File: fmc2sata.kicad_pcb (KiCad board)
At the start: 4 copper layers, 108 x 69 mm, 58 parts, among them J1 ASP-134488-01, J2 1-2199230-6, J3 te-770829-1, Q1 BSS138APW, Q2 BSS138APW, Q3 DMG2305UX-13, Q4 BSS138APW, U1 TPS565208, U2 TPS565208, Y1 AX3DAF1-150.0000

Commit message: Component cleanup
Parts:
- C1, C2, C3, C6, C7, C8: footprint antmicro-footprints:0603-cap -> fmc2sata-footprints:0603-cap
- C10, C4, C5, C9: footprint antmicro-footprints:0805-cap -> fmc2sata-footprints:0805-cap
- D1, D2, D3, D4, D5: footprint antmicro-footprints:LED_0603 -> fmc2sata-footprints:LED_0603
- J1: footprint antmicro-footprints:ASP-134488-01 -> fmc2sata-footprints:ASP-134488-01
- J2: footprint antmicro-footprints:1-2199230-6 -> fmc2sata-footprints:1-2199230-6
- J3: footprint antmicro-footprints:te-770829-1 -> fmc2sata-footprints:te-770829-1
- L1: footprint antmicro-footprints:WE_74437336022 -> fmc2sata-footprints:WE_74437336022
- L2: footprint antmicro-footprints:WE_74437336033 -> fmc2sata-footprints:WE_74437336033
- N1: footprint antmicro-footprints:antmicro-logo_scaled_20mm -> fmc2sata-footprints:antmicro-logo_scaled_20mm
- N2: footprint antmicro-footprints:oshw-logo -> fmc2sata-footprints:oshw-logo
- Q1, Q2, Q4: footprint antmicro-footprints:SC70-3 -> fmc2sata-footprints:SC70-3
- Q3: footprint antmicro-footprints:SOT-23-3 -> fmc2sata-footprints:SOT-23-3
- R1, R11, R12, R13, R17, R18, R19, R21, R22, R3, R4, R6, R7, R9: footprint antmicro-footprints:0402-res -> fmc2sata-footprints:0402-res
- SP1, SP2: footprint antmicro-footprints:9774025151 -> fmc2sata-footprints:9774025151
- U1, U2: footprint antmicro-footprints:SOT-23-6 -> fmc2sata-footprints:SOT-23-6
- Y1: footprint antmicro-footprints:AX3DAF1 -> fmc2sata-footprints:AX3DAF1

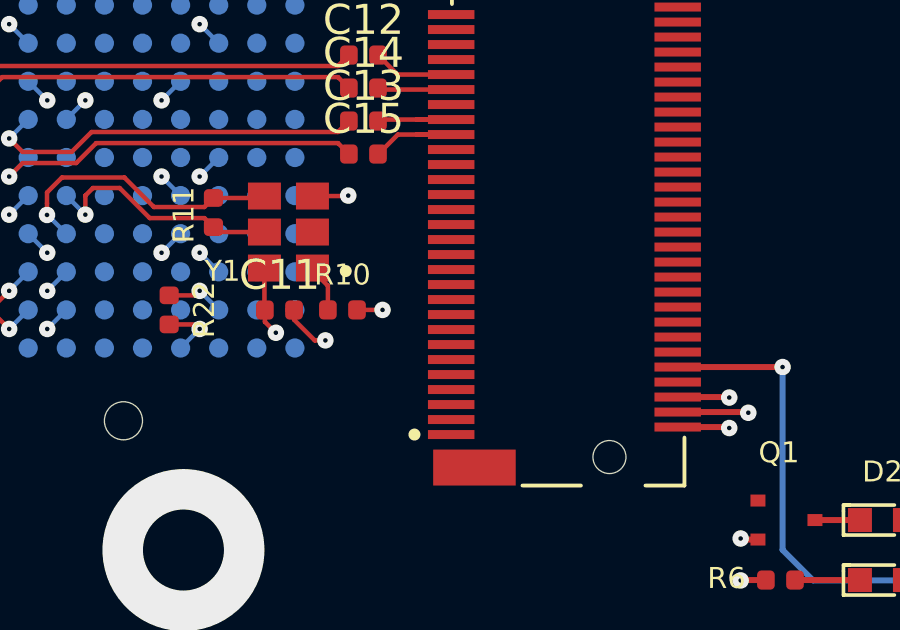
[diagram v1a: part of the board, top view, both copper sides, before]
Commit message: Update local libraries
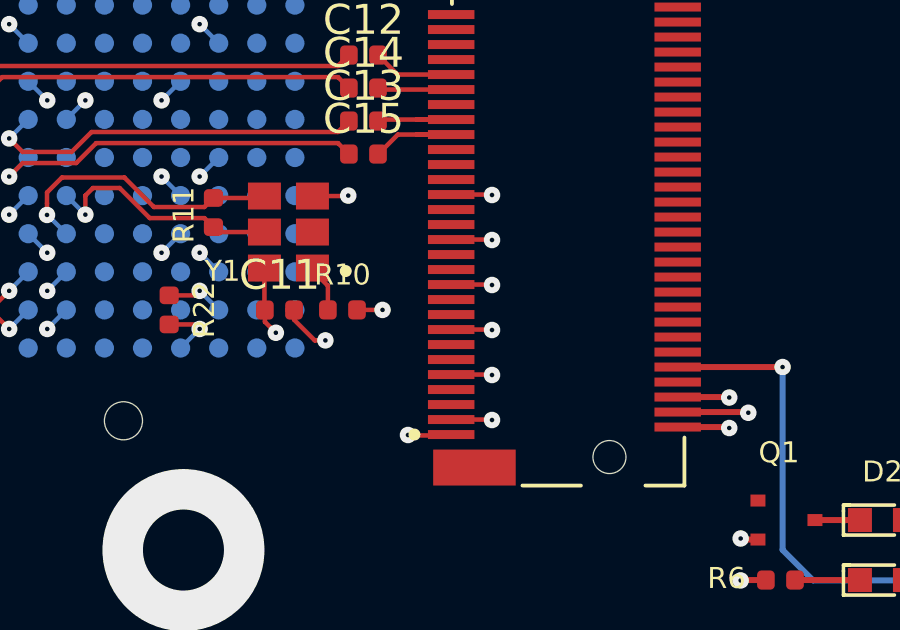
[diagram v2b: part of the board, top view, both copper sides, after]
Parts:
- C11, C12, C13, C14, C15: footprint antmicro-footprints:0402-cap -> fmc2sata-footprints:0402-cap
- R10, R14, R15, R16, R2, R20, R5, R8: footprint antmicro-footprints:0402-res -> fmc2sata-footprints:0402-res
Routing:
- net GND: track 69.0 -> 78.5 mm, vias 117 -> 124
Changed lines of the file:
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@@
     (thickness 1.6)
     (drawings 13)
-    (tracks 439)
+    (tracks 454)
     (zones 0)
     (modules 58)
@@
     (add_net SATA_CLK_P)
   )
-  (module antmicro-footprints:0402-res (layer F.Cu)
+  (module fmc2sata-footprints:0402-res (layer F.Cu)
     (at 128.606 66.424 270)
     (descr "Resistor SMD 0402 (1005 Metric), square (rectangular) end terminal, IPC_7351 nominal, (Body size source: http://www.tortai-tech.com/upload/download/2011102023233369053.pdf), generated with kicad-footprint-generator")
@@
     )
   )
-  (module antmicro-footprints:0402-res (layer F.Cu)
+  (module fmc2sata-footprints:0402-res (layer F.Cu)
     (at 105.3 66.7)
     (descr "Resistor SMD 0402 (1005 Metric), square (rectangular) end terminal, IPC_7351 nominal, (Body size source: http://www.tortai-tech.com/upload/download/2011102023233369053.pdf), generated with kicad-footprint-generator")
@@
     )
   )
-  (module antmicro-footprints:0402-res (layer F.Cu)
+  (module fmc2sata-footprints:0402-res (layer F.Cu)
     (at 105.3 68.7 180)
     (descr "Resistor SMD 0402 (1005 Metric), square (rectangular) end terminal, IPC_7351 nominal, (Body size source: http://www.tortai-tech.com/upload/download/2011102023233369053.pdf), generated with kicad-footprint-generator")
@@
     )
   )
-  (module antmicro-footprints:0402-res (layer F.Cu)
+  (module fmc2sata-footprints:0402-res (layer F.Cu)
     (at 105.3 69.8)
     (descr "Resistor SMD 0402 (1005 Metric), square (rectangular) end terminal, IPC_7351 nominal, (Body size source: http://www.tortai-tech.com/upload/download/2011102023233369053.pdf), generated with kicad-footprint-generator")
@@
     )
   )
-  (module antmicro-footprints:0402-res (layer F.Cu)
+  (module fmc2sata-footprints:0402-res (layer F.Cu)
     (at 87.9 101.095)
     (descr "Resistor SMD 0402 (1005 Metric), square (rectangular) end terminal, IPC_7351 nominal, (Body size source: http://www.tortai-tech.com/upload/download/2011102023233369053.pdf), generated with kicad-footprint-generator")
@@
     )
   )
-  (module antmicro-footprints:0402-res (layer F.Cu)
+  (module fmc2sata-footprints:0402-res (layer F.Cu)
     (at 85.6 84.9)
     (descr "Resistor SMD 0402 (1005 Metric), square (rectangular) end terminal, IPC_7351 nominal, (Body size source: http://www.tortai-tech.com/upload/download/2011102023233369053.pdf), generated with kicad-footprint-generator")
@@
     )
   )
-  (module antmicro-footprints:0402-res (layer F.Cu)
+  (module fmc2sata-footprints:0402-res (layer F.Cu)
     (at 99.5 62.47 90)
     (descr "Resistor SMD 0402 (1005 Metric), square (rectangular) end terminal, IPC_7351 nominal, (Body size source: http://www.tortai-tech.com/upload/download/2011102023233369053.pdf), generated with kicad-footprint-generator")
@@
     )
   )
-  (module antmicro-footprints:0402-res (layer F.Cu)
+  (module fmc2sata-footprints:0402-res (layer F.Cu)
     (at 99.63 76.51 90)
     (descr "Resistor SMD 0402 (1005 Metric), square (rectangular) end terminal, IPC_7351 nominal, (Body size source: http://www.tortai-tech.com/upload/download/2011102023233369053.pdf), generated with kicad-footprint-generator")
@@
     )
   )
-  (module antmicro-footprints:0402-cap (layer F.Cu)
+  (module fmc2sata-footprints:0402-cap (layer F.Cu)
     (at 88.6 95.9)
     (descr "Resistor SMD 0402 (1005 Metric), square (rectangular) end terminal, IPC_7351 nominal, (Body size source: http://www.tortai-tech.com/upload/download/2011102023233369053.pdf), generated with kicad-footprint-generator")
@@
     )
   )
-  (module antmicro-footprints:0402-cap (layer F.Cu)
+  (module fmc2sata-footprints:0402-cap (layer F.Cu)
     (at 88.6 93.7)
     (descr "Resistor SMD 0402 (1005 Metric), square (rectangular) end terminal, IPC_7351 nominal, (Body size source: http://www.tortai-tech.com/upload/download/2011102023233369053.pdf), generated with kicad-footprint-generator")
@@
     )
   )
-  (module antmicro-footprints:0402-cap (layer F.Cu)
+  (module fmc2sata-footprints:0402-cap (layer F.Cu)
     (at 88.6 94.8)
     (descr "Resistor SMD 0402 (1005 Metric), square (rectangular) end terminal, IPC_7351 nominal, (Body size source: http://www.tortai-tech.com/upload/download/2011102023233369053.pdf), generated with kicad-footprint-generator")
@@
     )
   )
-  (module antmicro-footprints:0402-cap (layer F.Cu)
+  (module fmc2sata-footprints:0402-cap (layer F.Cu)
     (at 88.6 92.6)
     (descr "Resistor SMD 0402 (1005 Metric), square (rectangular) end terminal, IPC_7351 nominal, (Body size source: http://www.tortai-tech.com/upload/download/2011102023233369053.pdf), generated with kicad-footprint-generator")
@@
     )
   )
-  (module antmicro-footprints:0402-cap (layer F.Cu)
+  (module fmc2sata-footprints:0402-cap (layer F.Cu)
     (at 85.8 101.1)
     (descr "Resistor SMD 0402 (1005 Metric), square (rectangular) end terminal, IPC_7351 nominal, (Body size source: http://www.tortai-tech.com/upload/download/2011102023233369053.pdf), generated with kicad-footprint-generator")
@@
   (via (at 132.602 46.1) (size 5.4) (drill 2.7) (layers F.Cu B.Cu) (net 0))
   (via (at 132.6 109.1) (size 5.5) (drill 2.7) (layers F.Cu B.Cu) (net 0))
+  (via (at 90.085 105.265) (size 0.55) (drill 0.15) (layers F.Cu B.Cu) (net 2))
+  (segment (start 91.445 105.28) (end 90.1 105.28) (width 0.15) (layer F.Cu) (net 2))
+  (via (at 92.885 104.765) (size 0.55) (drill 0.15) (layers F.Cu B.Cu) (net 2))
+  (segment (start 91.525 104.75) (end 92.87 104.75) (width 0.15) (layer F.Cu) (net 2))
+  (via (at 92.885 103.265) (size 0.55) (drill 0.15) (layers F.Cu B.Cu) (net 2))
+  (segment (start 91.525 103.25) (end 92.87 103.25) (width 0.15) (layer F.Cu) (net 2))
+  (via (at 92.885 101.765) (size 0.55) (drill 0.15) (layers F.Cu B.Cu) (net 2))
+  (segment (start 91.525 101.75) (end 92.87 101.75) (width 0.15) (layer F.Cu) (net 2))
+  (via (at 92.885 100.265) (size 0.55) (drill 0.15) (layers F.Cu B.Cu) (net 2))
+  (segment (start 91.525 100.25) (end 92.87 100.25) (width 0.15) (layer F.Cu) (net 2))
+  (via (at 92.885 98.765) (size 0.55) (drill 0.15) (layers F.Cu B.Cu) (net 2))
+  (segment (start 91.525 98.75) (end 92.87 98.75) (width 0.15) (layer F.Cu) (net 2))
   (segment (start 77.425 54.105) (end 76.79 53.47) (width 0.15) (layer B.Cu) (net 1))
   (via (at 76.79 53.47) (size 0.55) (drill 0.15) (layers F.Cu B.Cu) (net 1))
@@
   (segment (start 126.64 69.25) (end 127.177 69.25) (width 0.15) (layer F.Cu) (net 2))
   (segment (start 127.177 69.25) (end 127.209 69.218) (width 0.15) (layer F.Cu) (net 2))
+  (via (at 92.885 97.265) (size 0.55) (drill 0.15) (layers F.Cu B.Cu) (net 2))
+  (segment (start 91.525 97.25) (end 92.87 97.25) (width 0.15) (layer F.Cu) (net 2))
+  (segment (start 92.87 97.25) (end 92.885 97.265) (width 0.15) (layer F.Cu) (net 2))
   (segment (start 94.85 76.03) (end 93.85 76.03) (width 0.5) (layer F.Cu) (net 3))
   (segment (start 95.16 75.72) (end 94.85 76.03) (width 0.5) (layer F.Cu) (net 3))

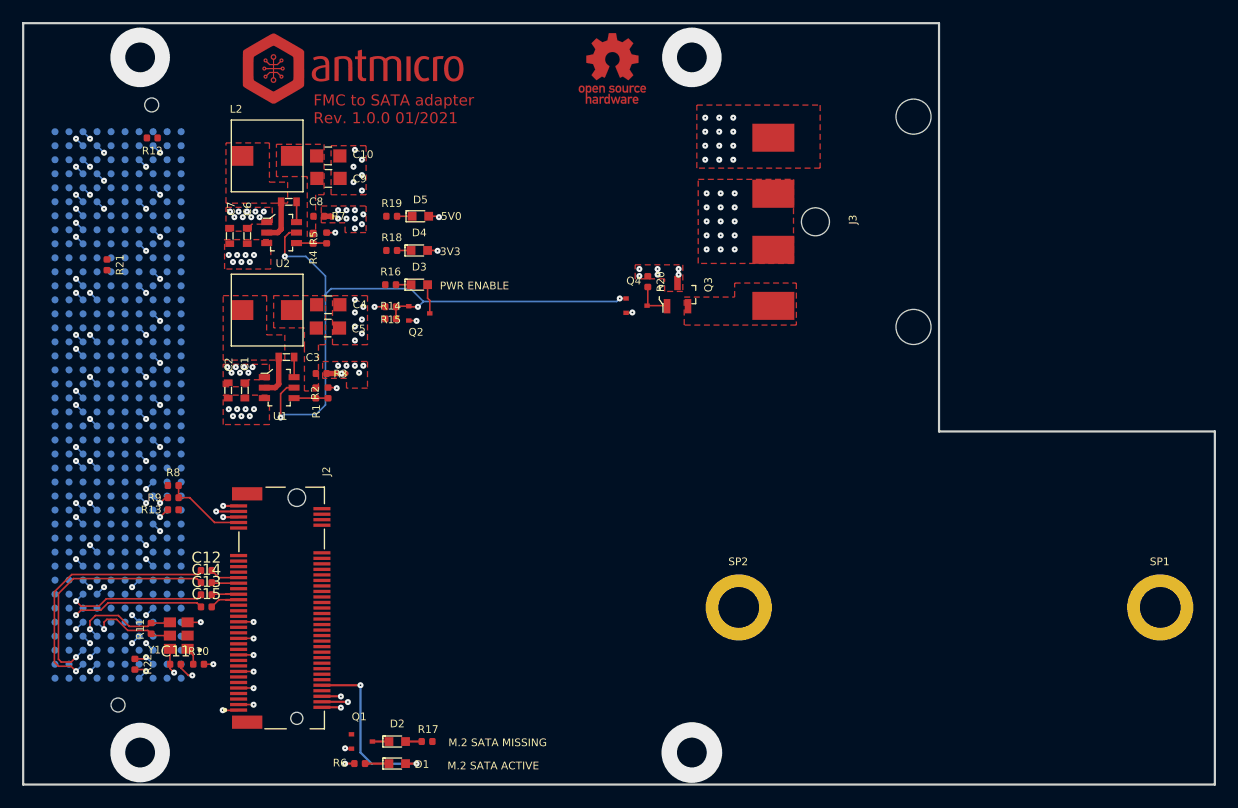
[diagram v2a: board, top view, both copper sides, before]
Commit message: All signals connected, DRC clean
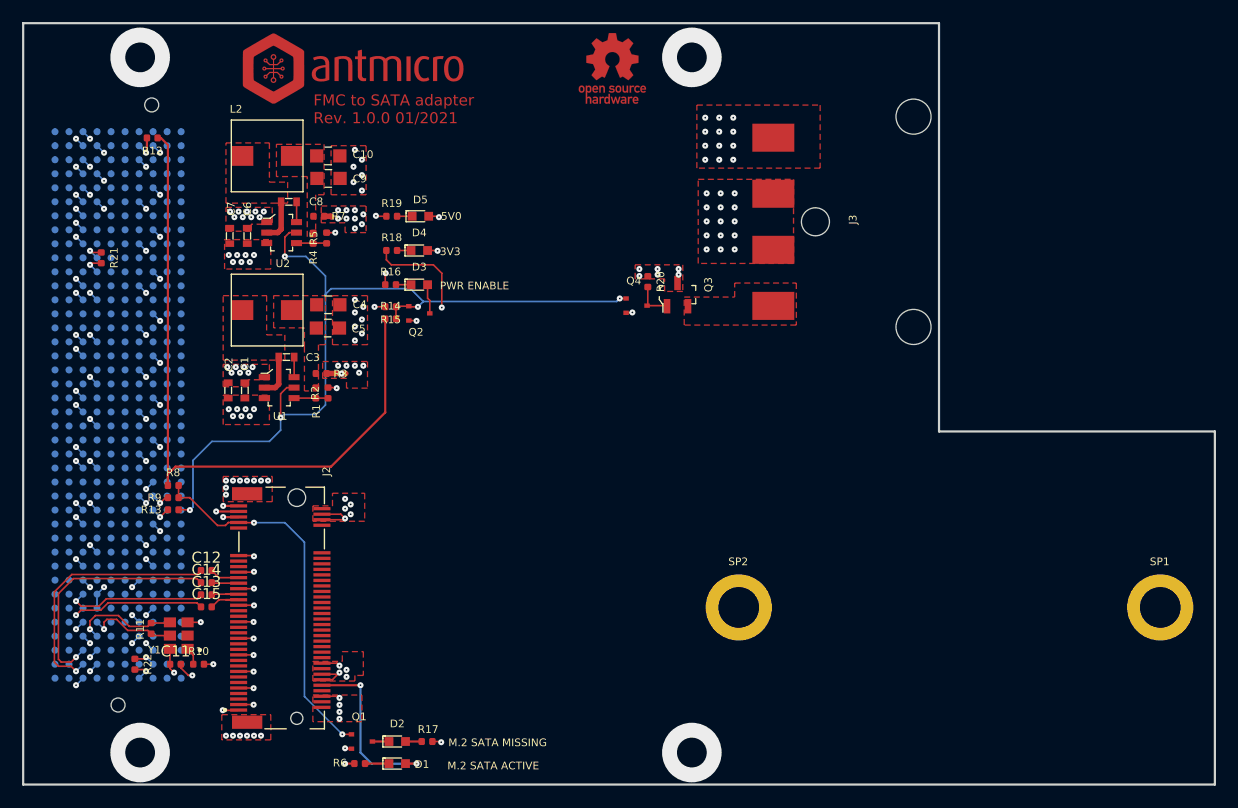
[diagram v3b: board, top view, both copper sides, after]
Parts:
- moved R21 0.82 mm to (79.1, 64.3)
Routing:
- net VCC_IO: track 0.00 -> 63.6 mm
- net SATA_FLAG: track 7.47 -> 34.1 mm, vias 0 -> 2
- net PWR_EN: track 59.2 -> 75.1 mm, vias 4 -> 5
- net +3V3: track 11.6 -> 27.3 mm, vias 12 -> 24
- net GND: track 78.5 -> 86.3 mm, vias 124 -> 144
- net Net-(J1-PadG39): track 0.00 -> 2.27 mm, vias 0 -> 1
- net /JTAG_TDI: track 0.00 -> 1.98 mm, vias 0 -> 1
- net /JTAG_TDO: track 0.00 -> 1.98 mm, vias 0 -> 1
- net +12V: track 2.69 -> 3.75 mm, vias 23 -> 24
- net +5V: track 0.72 -> 1.69 mm, vias 21 -> 22
- added copper zone on In2.Cu, net +3V3
- added copper zone on In2.Cu, net GND

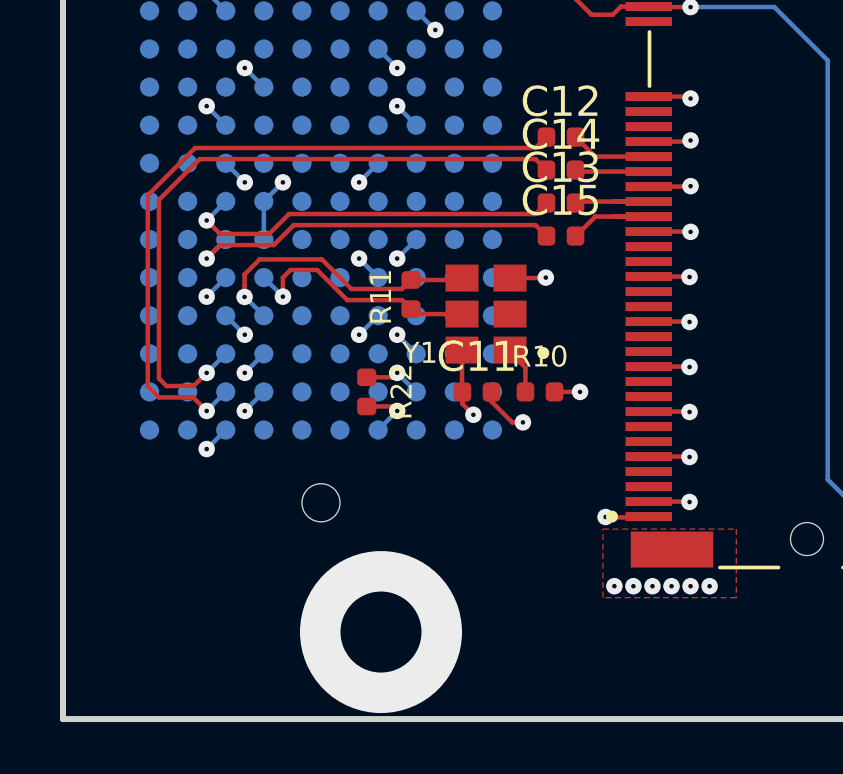
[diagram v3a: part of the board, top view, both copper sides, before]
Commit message: Add length tunning
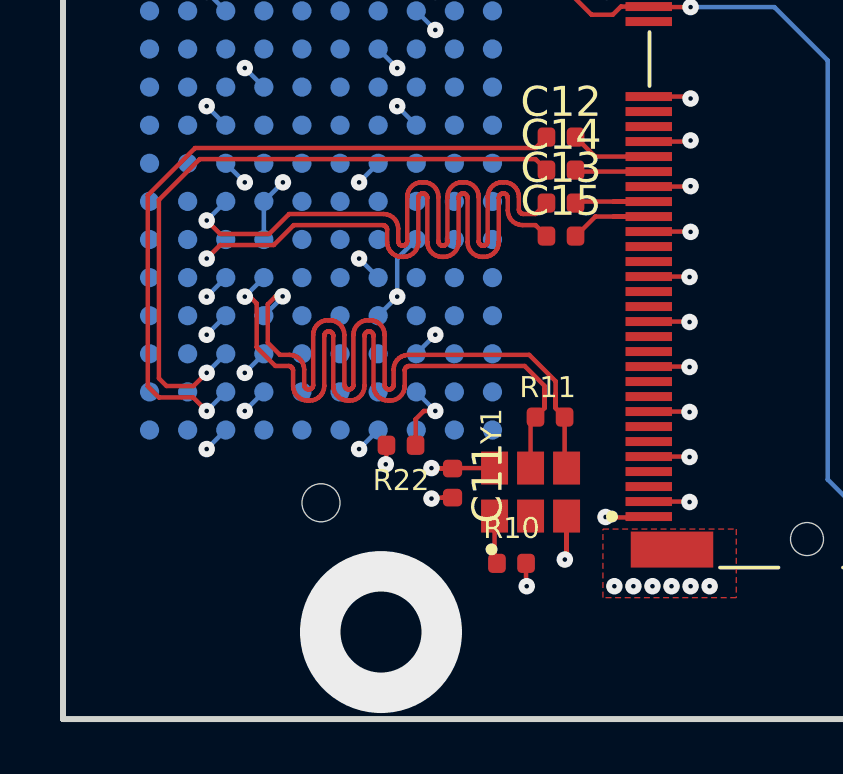
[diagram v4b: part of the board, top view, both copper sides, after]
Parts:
- moved R11 6.18 mm to (88.2, 101.9), turned to 180 degrees
- moved Y1 6.12 mm to (87.6, 104.4), turned to 0 degrees
- moved R10 5.79 mm to (87.0, 106.8)
- moved C11 3.14 mm to (85.0, 104.1), turned to 270 degrees
- moved R22 2.11 mm to (83.3, 102.9), turned to 180 degrees
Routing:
- net SATA_CLK_N: track 8.22 -> 26.4 mm
- net SATA_CLK_P: track 9.69 -> 26.7 mm
- net SATA_B_P: track 12.8 -> 23.6 mm
- net SATA_B_N: track 12.8 -> 23.6 mm
- net GND: track 86.3 -> 88.0 mm
- net /PRSNT: track 1.98 -> 2.54 mm
